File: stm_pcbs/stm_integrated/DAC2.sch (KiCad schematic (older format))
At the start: 21 parts, among them P1 BNC, U1 AD8676, U2 AD5791, U3 AD8675

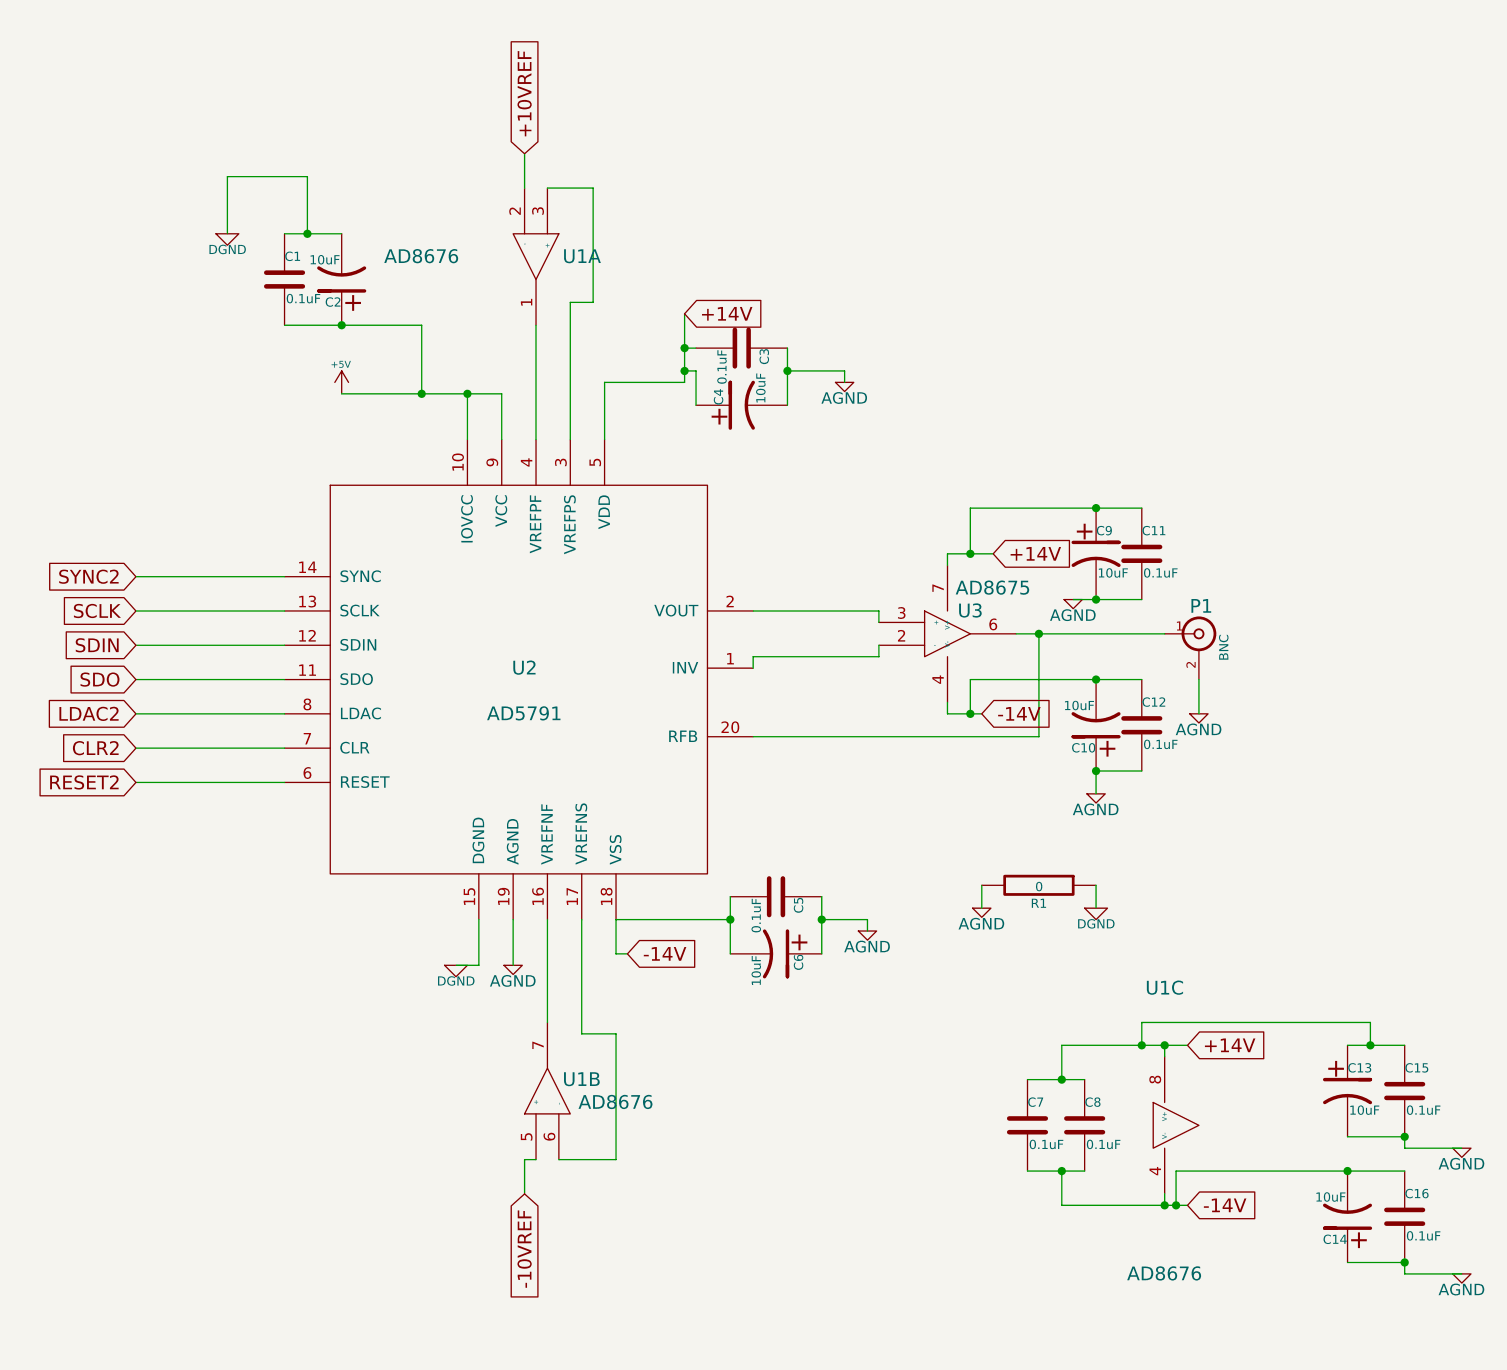
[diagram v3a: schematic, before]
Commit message: fixed issue with DAC (opamp wiring was wrong)
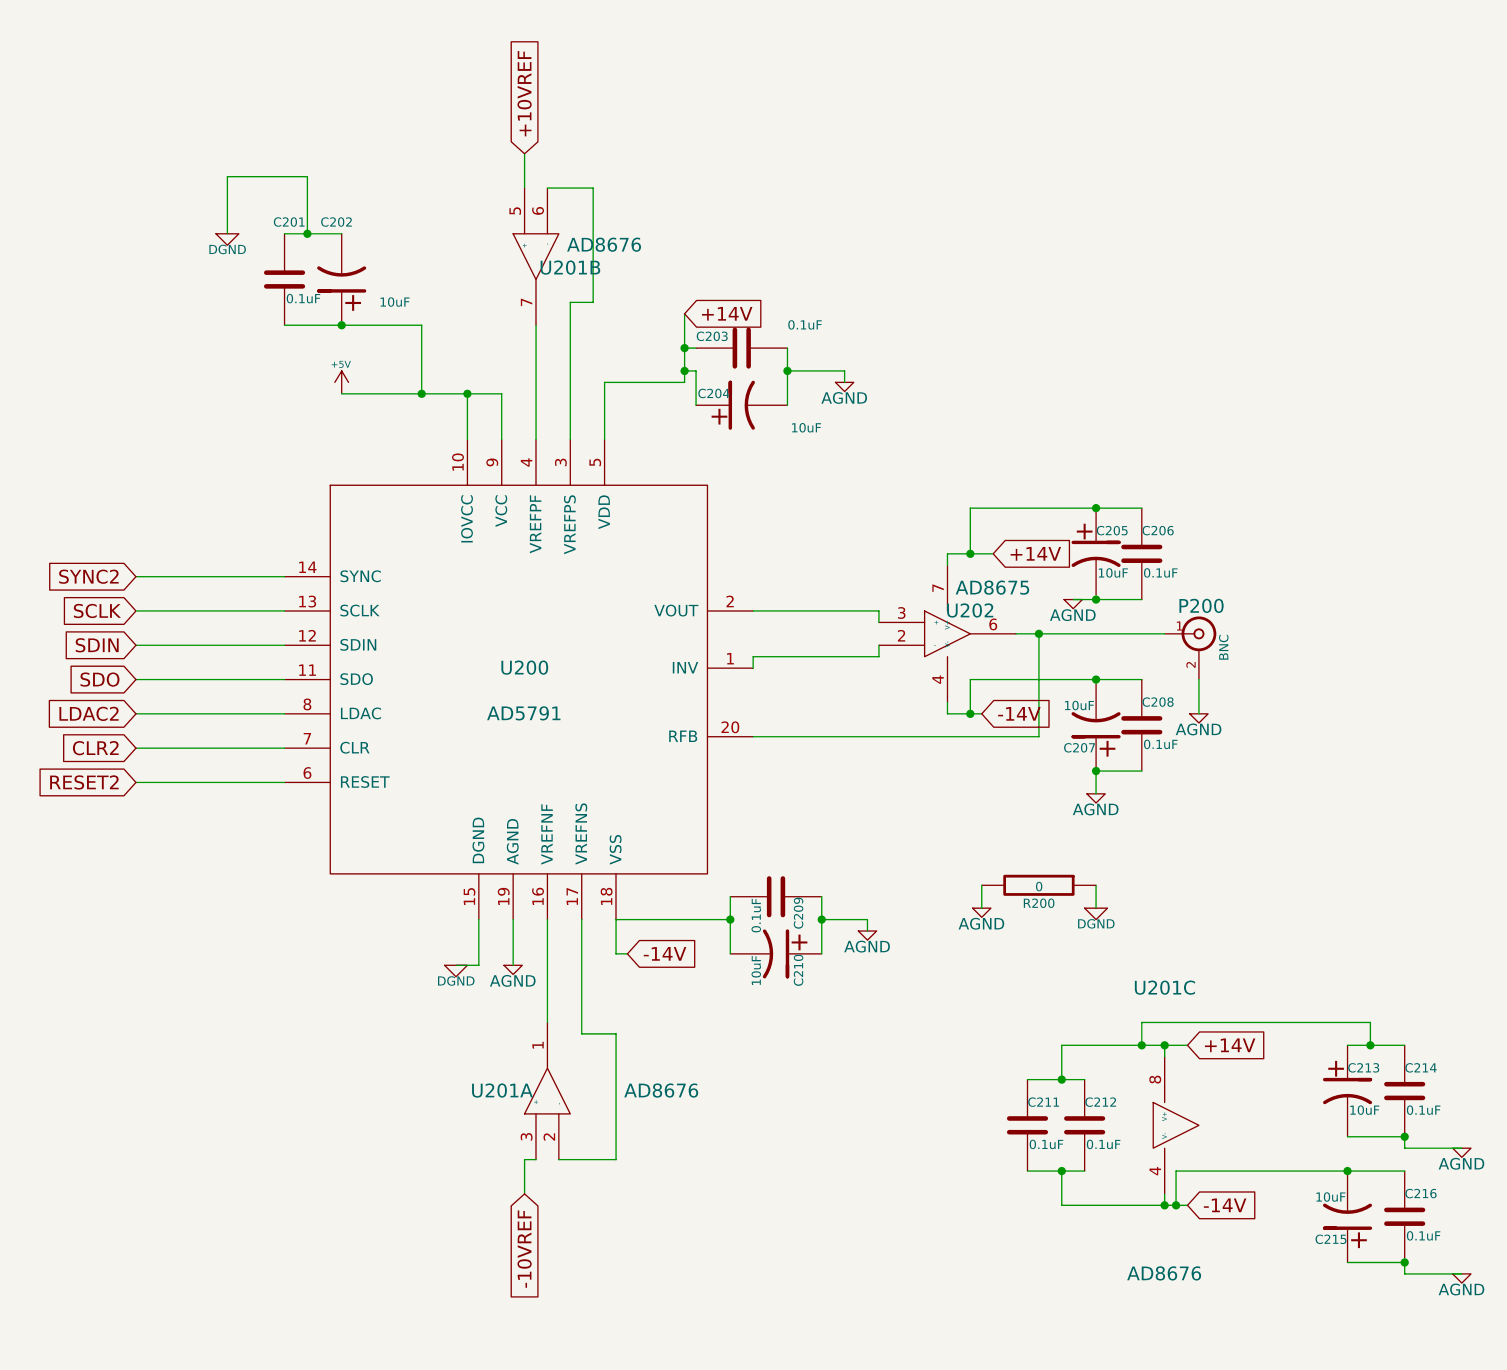
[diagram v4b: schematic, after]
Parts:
- renumbered C1 to C201, C2 to C202, C3 to C203, C4 to C204, C9 to C205, C11 to C206, C10 to C207, C12 to C208, C5 to C209, C6 to C210, C7 to C211, C8 to C212, C13 to C213, C15 to C214, C14 to C215, C16 to C216, P1 to P200, R1 to R200, U2 to U200, U1 to U201, U3 to U202
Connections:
- net +10VREF: now also U201.5 (+); no longer U201.2 (-)
- net -10VREF: now also U201.3 (+); no longer U201.5 (+)
- net at U200.16 (VREFNF): now also U201.1; no longer U201.7
- net at U200.17 (VREFNS): now also U201.2 (-); no longer U201.6 (-)
- net at U200.3 (VREFPS): now also U201.6 (-); no longer U201.3 (+)
- net at U200.4 (VREFPF): now also U201.7; no longer U201.1
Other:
- moved on the sheet: U201A, U201B
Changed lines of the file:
@@
 $EndDescr
 $Comp
-L ad5791:AD5791 U2
+L ad5791:AD5791 U200
 U 1 1 5A25EB42
 P 5050 3750
-F 0 "U2" H 4900 3950 60  0000 C CNN
+F 0 "U200" H 4900 3950 60  0000 C CNN
 F 1 "AD5791" H 4900 3750 60  0000 C CNN
 F 2 "stm:SSOP-20" H 5050 3800 60  0001 C CNN
@@
 $EndComp
 $Comp
-L ad5791:AD8675 U3
+L ad5791:AD8675 U202
 U 1 1 5A25EB49
 P 6750 3400
-F 0 "U3" H 6850 3500 60  0000 C CNN
+F 0 "U202" H 6850 3500 60  0000 C CNN
 F 1 "AD8675" H 6950 3600 60  0000 C CNN
 F 2 "stm:SOIC-8" H 6950 3350 60  0001 C CNN
@@
 $EndComp
 $Comp
-L ad5791:AD8676 U1
+L ad5791:AD8676 U201
 U 1 1 5A25EB50
+P 5000 5450
+F 0 "U201" V 5050 5650 60  0000 C CNN
+F 1 "AD8676" V 5050 4950 60  0000 C CNN
+F 2 "stm:SOIC-8" H 5150 5450 60  0001 C CNN
+F 3 "" H 5150 5450 60  0000 C CNN
+	1    5000 5450
+	0    -1   -1   0
+$EndComp
+$Comp
+L ad5791:AD8676 U201
+U 2 1 5A25EB57
 P 4950 1700
-F 0 "U1" V 5000 1900 60  0000 C CNN
-F 1 "AD8676" V 5000 1200 60  0000 C CNN
+F 0 "U201" V 5050 1550 60  0000 C CNN
+F 1 "AD8676" V 4950 1400 60  0000 C CNN
 F 2 "stm:SOIC-8" H 5100 1700 60  0001 C CNN
 F 3 "" H 5100 1700 60  0000 C CNN
-	1    4950 1700
-	0    1    1    0
-$EndComp
-$Comp
-L ad5791:AD8676 U1
-U 2 1 5A25EB57
-P 5000 5450
-F 0 "U1" V 5100 5300 60  0000 C CNN
-F 1 "AD8676" V 5000 5150 60  0000 C CNN
-F 2 "stm:SOIC-8" H 5150 5450 60  0001 C CNN
-F 3 "" H 5150 5450 60  0000 C CNN
-	2    5000 5450
-	0    -1   -1   0
-$EndComp
-$Comp
-L ad5791:AD8676 U1
+	2    4950 1700
+	0    -1   1    0
+$EndComp
+$Comp
+L ad5791:AD8676 U201
 U 3 1 5A25EB5E
 P 7700 5550
-F 0 "U1" H 7700 6150 60  0000 C CNN
+F 0 "U201" H 7700 6150 60  0000 C CNN
 F 1 "AD8676" H 7700 4900 60  0000 C CNN
 F 2 "stm:SOIC-8" H 7850 5550 60  0001 C CNN
@@
 $EndComp
 $Comp
-L device:BNC P1
+L device:BNC P200
 U 1 1 5A25EB65
 P 7850 3400
-F 0 "P1" H 7860 3520 60  0000 C CNN
+F 0 "P200" H 7860 3520 60  0000 C CNN
 F 1 "BNC" V 7960 3340 40  0000 C CNN
 F 2 "stm:SMA" H 7850 3400 60  0001 C CNN
@@
 $EndComp
 $Comp
-L device:C C3
+L device:C C203
 U 1 1 5A25EB87
 P 5850 2150
-F 0 "C3" H 5850 2250 40  0000 L CNN
-F 1 "0.1uF" H 5856 2065 40  0000 L CNN
+F 0 "C203" V 5800 1950 40  0000 L CNN
+F 1 "0.1uF" V 5750 2350 40  0000 L CNN
 F 2 "Capacitors_SMD:C_0805_HandSoldering" H 5888 2000 30  0001 C CNN
 F 3 "" H 5850 2150 60  0000 C CNN
@@
 $EndComp
 $Comp
-L device:C C5
+L device:C C209
 U 1 1 5A25EB94
 P 6000 4550
-F 0 "C5" H 6000 4650 40  0000 L CNN
+F 0 "C209" H 6000 4650 40  0000 L CNN
 F 1 "0.1uF" H 6006 4465 40  0000 L CNN
 F 2 "Capacitors_SMD:C_0805_HandSoldering" H 6038 4400 30  0001 C CNN
@@
 $EndComp
 $Comp
-L device:C C1
+L device:C C201
 U 1 1 5A25EBAF
 P 3850 1850
-F 0 "C1" H 3850 1950 40  0000 L CNN
+F 0 "C201" H 3800 2100 40  0000 L CNN
 F 1 "0.1uF" H 3856 1765 40  0000 L CNN
 F 2 "Capacitors_SMD:C_0805_HandSoldering" H 3888 1700 30  0001 C CNN
@@
 $EndComp
 $Comp
-L device:C C8
+L device:C C212
 U 1 1 5A25EBBC
 P 7350 5550
-F 0 "C8" H 7350 5650 40  0000 L CNN
+F 0 "C212" H 7350 5650 40  0000 L CNN
 F 1 "0.1uF" H 7356 5465 40  0000 L CNN
 F 2 "Capacitors_SMD:C_0805_HandSoldering" H 7388 5400 30  0001 C CNN
@@
 $EndComp
 $Comp
-L device:C C15
+L device:C C214
 U 1 1 5A25EBC3
 P 8750 5400
-F 0 "C15" H 8750 5500 40  0000 L CNN
+F 0 "C214" H 8750 5500 40  0000 L CNN
 F 1 "0.1uF" H 8756 5315 40  0000 L CNN
 F 2 "Capacitors_SMD:C_0805_HandSoldering" H 8788 5250 30  0001 C CNN
@@
 $EndComp
 $Comp
-L device:C C16
+L device:C C216
 U 1 1 5A25EBCA
 P 8750 5950
-F 0 "C16" H 8750 6050 40  0000 L CNN
+F 0 "C216" H 8750 6050 40  0000 L CNN
 F 1 "0.1uF" H 8756 5865 40  0000 L CNN
 F 2 "Capacitors_SMD:C_0805_HandSoldering" H 8788 5800 30  0001 C CNN
@@
 $EndComp
 $Comp
-L device:C C7
+L device:C C211
 U 1 1 5A25EBDD
 P 7100 5550
-F 0 "C7" H 7100 5650 40  0000 L CNN
+F 0 "C211" H 7100 5650 40  0000 L CNN
 F 1 "0.1uF" H 7106 5465 40  0000 L CNN
 F 2 "Capacitors_SMD:C_0805_HandSoldering" H 7138 5400 30  0001 C CNN
@@
 $EndComp
 $Comp
-L device:CP1 C13
+L device:CP1 C213
 U 1 1 5A25EBE4
 P 8500 5400
-F 0 "C13" H 8500 5500 40  0000 L CNN
+F 0 "C213" H 8500 5500 40  0000 L CNN
 F 1 "10uF" H 8506 5315 40  0000 L CNN
 F 2 "stm:SMD-1210_Pol" H 8538 5250 30  0001 C CNN
@@
 $EndComp
 $Comp
-L device:CP1 C14
+L device:CP1 C215
 U 1 1 5A25EBEB
 P 8500 5950
-F 0 "C14" H 8500 6050 40  0000 L CNN
+F 0 "C215" H 8500 6050 40  0000 L CNN
 F 1 "10uF" H 8506 5865 40  0000 L CNN
 F 2 "stm:SMD-1210_Pol" H 8538 5800 30  0001 C CNN
@@
 $EndComp
 $Comp
-L device:CP1 C6
+L device:CP1 C210
 U 1 1 5A25EBF2
 P 6000 4800
-F 0 "C6" H 6000 4900 40  0000 L CNN
+F 0 "C210" H 6000 4900 40  0000 L CNN
 F 1 "10uF" H 6006 4715 40  0000 L CNN
 F 2 "stm:SMD-1210_Pol" H 6038 4650 30  0001 C CNN
@@
 $EndComp
 $Comp
-L device:CP1 C4
+L device:CP1 C204
 U 1 1 5A25EBF9
 P 5850 2400
-F 0 "C4" H 5850 2500 40  0000 L CNN
-F 1 "10uF" H 5856 2315 40  0000 L CNN
+F 0 "C204" V 5900 2450 40  0000 L CNN
+F 1 "10uF" V 5750 2050 40  0000 L CNN
 F 2 "stm:SMD-1210_Pol" H 5888 2250 30  0001 C CNN
 F 3 "" H 5850 2400 60  0000 C CNN
@@
 $EndComp
 $Comp
-L device:CP1 C2
+L device:CP1 C202
 U 1 1 5A25EC00
 P 4100 1850
-F 0 "C2" H 4100 1950 40  0000 L CNN
-F 1 "10uF" H 4106 1765 40  0000 L CNN
+F 0 "C202" H 4050 1600 40  0000 L CNN
+F 1 "10uF" H 3800 1950 40  0000 L CNN
 F 2 "stm:SMD-1210_Pol" H 4138 1700 30  0001 C CNN
 F 3 "" H 4100 1850 60  0000 C CNN
@@
 RESET2
 $Comp
-L device:CP1 C9
+L device:CP1 C205
 U 1 1 5A25EC0E
 P 7400 3050
-F 0 "C9" H 7400 3150 40  0000 L CNN
+F 0 "C205" H 7400 3150 40  0000 L CNN
 F 1 "10uF" H 7406 2965 40  0000 L CNN
 F 2 "stm:SMD-1210_Pol" H 7438 2900 30  0001 C CNN
@@
 $EndComp
 $Comp
-L device:CP1 C10
+L device:CP1 C207
 U 1 1 5A25EC15
 P 7400 3800
-F 0 "C10" H 7400 3900 40  0000 L CNN
+F 0 "C207" H 7400 3900 40  0000 L CNN
 F 1 "10uF" H 7406 3715 40  0000 L CNN
 F 2 "stm:SMD-1210_Pol" H 7438 3650 30  0001 C CNN
@@
 $EndComp
 $Comp
-L device:C C11
+L device:C C206
 U 1 1 5A25EC1C
 P 7600 3050
-F 0 "C11" H 7600 3150 40  0000 L CNN
+F 0 "C206" H 7600 3150 40  0000 L CNN
 F 1 "0.1uF" H 7606 2965 40  0000 L CNN
 F 2 "Capacitors_SMD:C_0805_HandSoldering" H 7638 2900 30  0001 C CNN
@@
 $EndComp
 $Comp
-L device:C C12
+L device:C C208
 U 1 1 5A25EC23
 P 7600 3800
-F 0 "C12" H 7600 3900 40  0000 L CNN
+F 0 "C208" H 7600 3900 40  0000 L CNN
 F 1 "0.1uF" H 7606 3715 40  0000 L CNN
 F 2 "Capacitors_SMD:C_0805_HandSoldering" H 7638 3650 30  0001 C CNN
@@
 	7850 3600 7850 3750
 Wire Wire Line
-	5600 2000 5600 2150
-Wire Wire Line
 	5300 4650 5300 4800
 Wire Wire Line
@@
 Wire Wire Line
 	5250 2300 5250 2550
-Wire Wire Line
-	5600 2150 5650 2150
-Connection ~ 5600 2150
 Wire Wire Line
 	5650 2400 5650 2250
@@
 Connection ~ 6850 3750
 $Comp
-L device:R R1
+L device:R R200
 U 1 1 5A25ECAA
 P 7150 4500
-F 0 "R1" V 7230 4500 40  0000 C CNN
+F 0 "R200" V 7230 4500 40  0000 C CNN
 F 1 "0" V 7157 4501 40  0000 C CNN
 F 2 "stm:0Ohm" V 7080 4500 30  0001 C CNN
@@
 	4650 2350 4800 2350
 Wire Wire Line
-	5600 2150 5600 2250
-Wire Wire Line
 	5600 2250 5600 2300
 Wire Wire Line
@@
 Wire Wire Line
 	4100 2350 4450 2350
+Wire Wire Line
+	5600 2150 5600 2250
+Wire Wire Line
+	5600 2000 5600 2150
+Connection ~ 5600 2150
+Wire Wire Line
+	5600 2150 5650 2150
 $EndSCHEMATC
